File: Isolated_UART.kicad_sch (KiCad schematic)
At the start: 32 parts, among them J1 Conn_01x03_Male, J2 USB_C_Receptacle_USB2.0, J3 Conn_01x10_Male, J4 Conn_01x03_Male, U1 USBLC6-2SC6, U2 ADuM1401xRW, U3 FT231XS-R, U4 ADuM1402xRW, U5 AP2127N-3.3

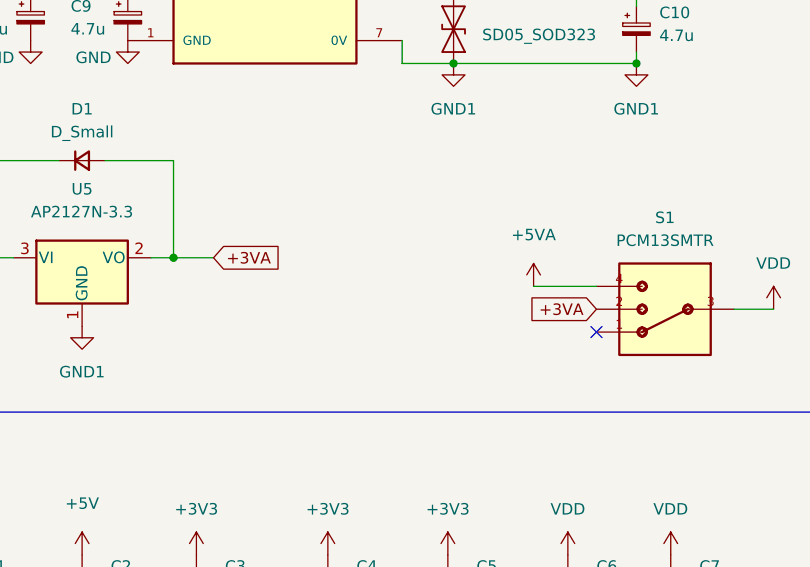
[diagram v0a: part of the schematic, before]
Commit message: Revised the schematic for clarity
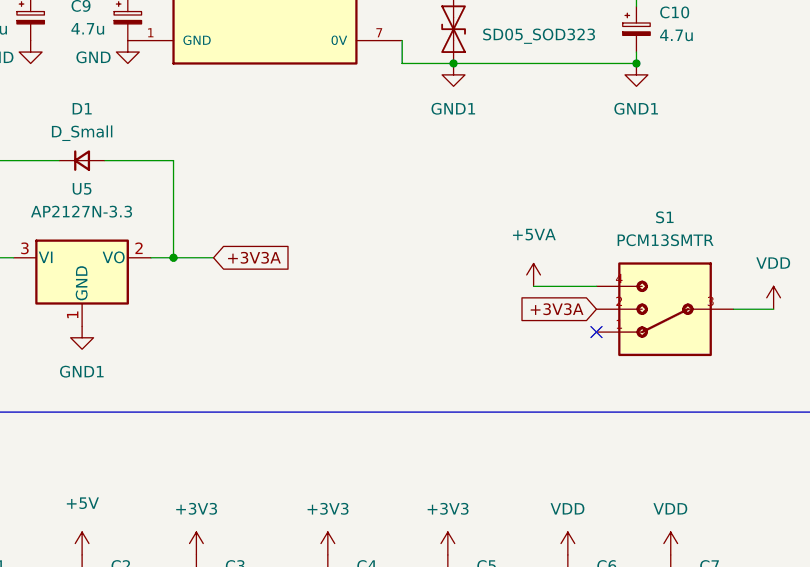
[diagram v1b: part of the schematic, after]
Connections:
- net +3VA renamed +3V3A
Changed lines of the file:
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@@
     )
   )
-  (global_label "+3VA" (shape input) (at 86.995 125.095 180) (fields_autoplaced)
+  (global_label "+3V3A" (shape input) (at 86.995 125.095 180) (fields_autoplaced)
     (effects (font (size 1.27 1.27)) (justify right))
-    (property "Intersheet References" "${INTERSHEET_REFS}" (id 0) (at 79.6229 125.1744 0)
+    (property "Intersheet References" "${INTERSHEET_REFS}" (id 0) (at 78.4133 125.0156 0)
       (effects (font (size 1.27 1.27)) (justify right) hide)
     )
@@
     )
   )
-  (global_label "+3VA" (shape input) (at 44.45 119.38 0) (fields_autoplaced)
+  (global_label "+3V3A" (shape input) (at 44.45 119.38 0) (fields_autoplaced)
     (effects (font (size 1.27 1.27)) (justify left))
-    (property "Intersheet References" "${INTERSHEET_REFS}" (id 0) (at 51.8221 119.3006 0)
+    (property "Intersheet References" "${INTERSHEET_REFS}" (id 0) (at 53.0317 119.3006 0)
       (effects (font (size 1.27 1.27)) (justify left) hide)
     )
